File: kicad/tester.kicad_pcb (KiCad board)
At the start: 2 copper layers, 95 x 89 mm, 0 parts

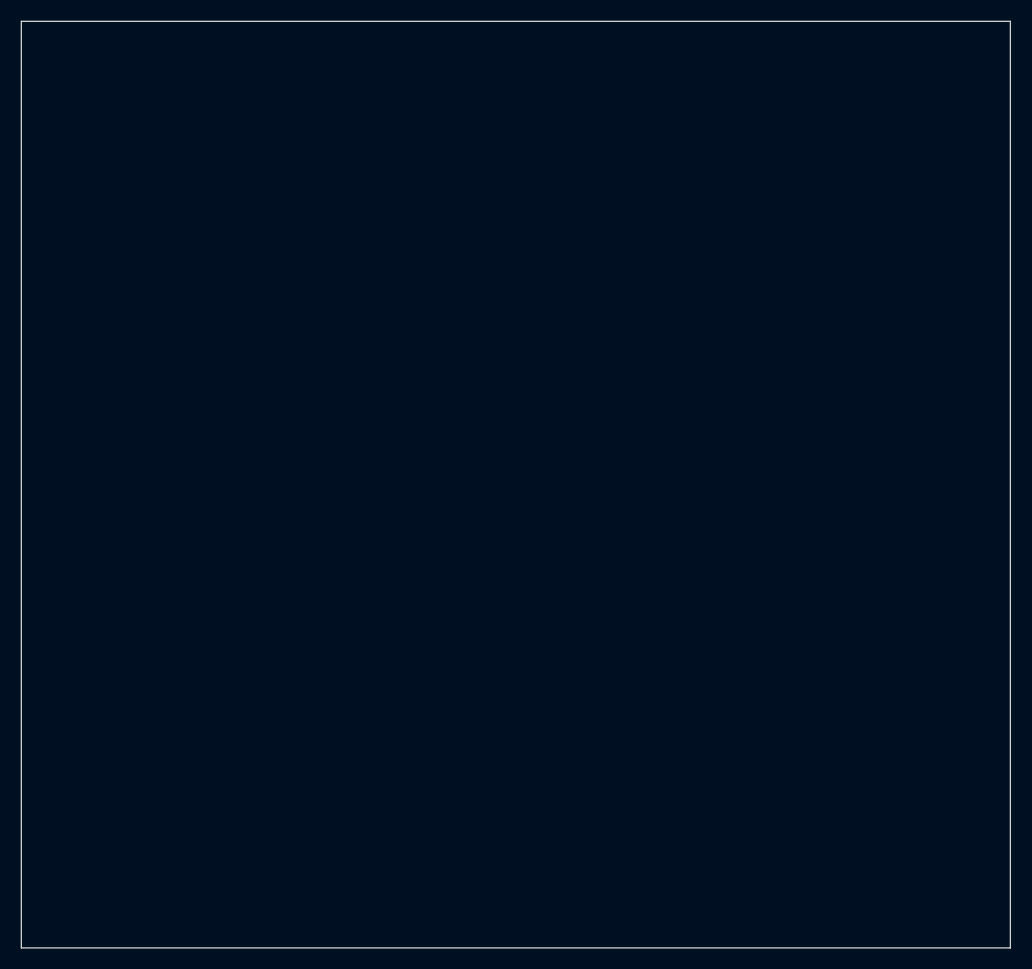
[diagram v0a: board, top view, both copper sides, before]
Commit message: Board routing almost done
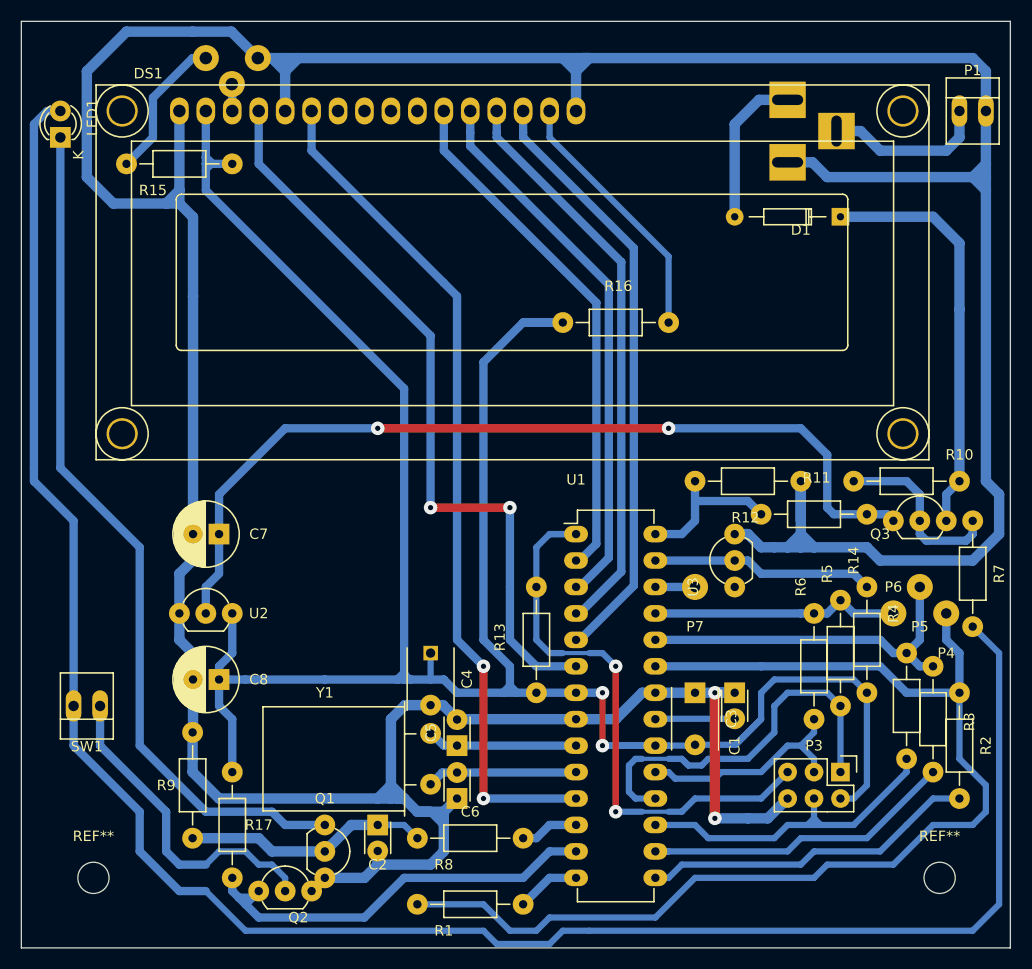
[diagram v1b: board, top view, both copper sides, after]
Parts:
- added C1: 1n, Capacitors_ThroughHole:C_Disc_D3_P2.5, F.Cu at (96.5, 110.5)
- added C2: 10n, Capacitors_ThroughHole:C_Disc_D3_P2.5, F.Cu at (62.2, 123.2)
- added C3: 100n, Capacitors_ThroughHole:C_Disc_D6_P5, F.Cu at (92.7, 110.5)
- added C4: 100n, Capacitors_ThroughHole:C_Disc_D6_P5, F.Cu at (67.3, 106.7)
- added C5: 22p, Capacitors_ThroughHole:C_Disc_D3_P2.5, F.Cu at (69.8, 115.6)
- added C6: 22p, Capacitors_ThroughHole:C_Disc_D3_P2.5, F.Cu at (69.8, 120.7)
- added C7: 2.2uF, Capacitors_ThroughHole:C_Radial_D6.3_L11.2_P2.5, F.Cu at (47.0, 95.2)
- added C8: 2.2uF, Capacitors_ThroughHole:C_Radial_D6.3_L11.2_P2.5, F.Cu at (47.0, 109.2)
- added D1: D_Small, Diodes_ThroughHole:Diode_DO-35_SOD27_Horizontal_RM10, F.Cu at (106.7, 64.8)
- added DS1: LCD16X2, Display:WC1602A, F.Cu at (43.2, 54.6)
- added LED1: Power, LEDs:LED-3MM, F.Cu at (31.8, 57.1)
- added P1: Battery 9V, Connect:PINHEAD1-2, F.Cu at (119.4, 54.6)
- added P2: 7-12 DC, Connect:BARREL_JACK, B.Cu at (101.6, 53.3)
- added P3: ISP, Pin_Headers:Pin_Header_Straight_2x03, F.Cu at (106.7, 118.1)
- added P4: TP1, Wire_Pads:SolderWirePad_single_1mmDrill, F.Cu at (116.8, 102.9)
- added P5: TP2, Wire_Pads:SolderWirePad_single_1mmDrill, F.Cu at (114.3, 100.3)
- added P6: TP3, Wire_Pads:SolderWirePad_single_1mmDrill, F.Cu at (111.8, 102.9)
- added P7: SERIAL, Wire_Pads:SolderWirePad_single_1mmDrill, F.Cu at (92.7, 100.3)
- added Q1: BC547, TO_SOT_Packages_THT:TO-92_Inline_Wide, F.Cu at (57.1, 123.2)
- added Q2: BC547, TO_SOT_Packages_THT:TO-92_Inline_Wide, F.Cu at (50.8, 129.5)
- added Q3: BC557, TO_SOT_Packages_THT:TO-92_Inline_Wide, F.Cu at (111.8, 94.0)
- added R1: 680, Resistors_ThroughHole:Resistor_Horizontal_RM10mm, F.Cu at (66.0, 130.8)
- added R10: 33K, Resistors_ThroughHole:Resistor_Horizontal_RM10mm, F.Cu at (118.1, 90.2)
- added R11: 10K, Resistors_ThroughHole:Resistor_Horizontal_RM10mm, F.Cu at (99.1, 93.3)
- added R12: 3K3, Resistors_ThroughHole:Resistor_Horizontal_RM10mm, F.Cu at (102.9, 90.2)
- added R13: 10k, Resistors_ThroughHole:Resistor_Horizontal_RM10mm, F.Cu at (77.5, 110.5)
- added R14: 2K2, Resistors_ThroughHole:Resistor_Horizontal_RM10mm, F.Cu at (109.2, 100.3)
- added R15: 10K, Resistors_ThroughHole:Resistor_Horizontal_RM10mm, F.Cu at (48.3, 59.7)
- added R16: 270, Resistors_ThroughHole:Resistor_Horizontal_RM10mm, F.Cu at (80.0, 74.9)
- added R17: 27K, Resistors_ThroughHole:Resistor_Horizontal_RM10mm, F.Cu at (48.3, 118.1)
- added R2: 470K, Resistors_ThroughHole:Resistor_Horizontal_RM10mm, F.Cu at (118.1, 110.5)
- added R3: 680, Resistors_ThroughHole:Resistor_Horizontal_RM10mm, F.Cu at (115.6, 108.0)
- added R4: 470K, Resistors_ThroughHole:Resistor_Horizontal_RM10mm, F.Cu at (113.0, 106.7)
- added R5: 680, Resistors_ThroughHole:Resistor_Horizontal_RM10mm, F.Cu at (106.7, 101.6)
- added R6: 470K, Resistors_ThroughHole:Resistor_Horizontal_RM10mm, F.Cu at (104.1, 102.9)
- added R7: 3K3, Resistors_ThroughHole:Resistor_Horizontal_RM10mm, F.Cu at (119.4, 94.0)
- added R8: 27K, Resistors_ThroughHole:Resistor_Horizontal_RM10mm, F.Cu at (66.0, 124.5)
- added R9: 100K, Resistors_ThroughHole:Resistor_Horizontal_RM10mm, F.Cu at (44.5, 124.5)
- added REF**: MountingHole_3mm, Mounting_Holes:MountingHole_3mm, F.Cu at (34.9, 128.3)
- added REF**: MountingHole_3mm, Mounting_Holes:MountingHole_3mm, F.Cu at (116.2, 128.3)
- added RV1: 5K, Potentiometers:Potentiometer_VishaySpectrol-Econtrim-Type36k, B.Cu at (45.7, 49.5)
- added SW1: TEST, Connect:PINHEAD1-2, F.Cu at (34.3, 111.8)
- added U1: ATMEGA328-P, Housings_DIP:DIP-28_W7.62mm_LongPads, F.Cu at (81.3, 95.2)
- added U2: MCP1702-5002E/TO, TO_SOT_Packages_THT:TO-92_Inline_Wide, F.Cu at (43.2, 102.9)
- added U3: LM336, TO_SOT_Packages_THT:TO-92_Inline_Wide, F.Cu at (96.5, 100.3)
- added Y1: 8MHz, Crystals:Crystal_HC49-U_Horizontal_Typ1, F.Cu at (67.3, 116.8)
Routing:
- net GND: track 0.00 -> 423.3 mm, vias 0 -> 2
- net VCC: track 0.00 -> 234.9 mm, vias 0 -> 2
- net Net-(LED1-Pad2): track 0.00 -> 192.7 mm
- net Net-(P4-Pad1): track 0.00 -> 111.3 mm
- net +9V: track 0.00 -> 86.0 mm, vias 0 -> 2
- net Net-(LED1-Pad1): track 0.00 -> 82.5 mm
- net Net-(DS1-Pad6): track 0.00 -> 82.1 mm, vias 0 -> 2
- net Net-(DS1-Pad4): track 0.00 -> 73.0 mm, vias 0 -> 2
- net Net-(DS1-Pad14): track 0.00 -> 57.7 mm
- net /RESET: track 0.00 -> 56.5 mm, vias 0 -> 2
- net Net-(DS1-Pad13): track 0.00 -> 55.2 mm
- net Net-(Q2-Pad1): track 0.00 -> 53.7 mm
- net Net-(DS1-Pad12): track 0.00 -> 52.7 mm
- net Net-(DS1-Pad11): track 0.00 -> 50.3 mm
- net Net-(D1-Pad1): track 0.00 -> 39.7 mm
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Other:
- net class Default: trace_width 0.25 -> 0.8
- net class Power added: clearance 0.2, trace_width 1, via_dia 1.3, via_drill 0.5
- net class Smaller added: clearance 0.2, trace_width 0.6, via_dia 0.6, via_drill 0.4

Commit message: * Minor changes
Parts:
- moved C8 19.4 mm to (57.1, 92.7)
- moved D1 14.4 mm to (96.5, 74.9), turned to 90 degrees
- moved C7 2.54 mm to (47.0, 92.7)
- moved U2 2.54 mm to (43.2, 100.3)
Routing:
- net GND: track 423.3 -> 461.8 mm
- net VCC: track 234.9 -> 261.5 mm
- net +9V: track 86.0 -> 85.0 mm
- net /Bat+: track 15.7 -> 16.7 mm
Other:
- net class Power2 added: clearance 0.2, trace_width 1.8, via_dia 0.6, via_drill 0.4

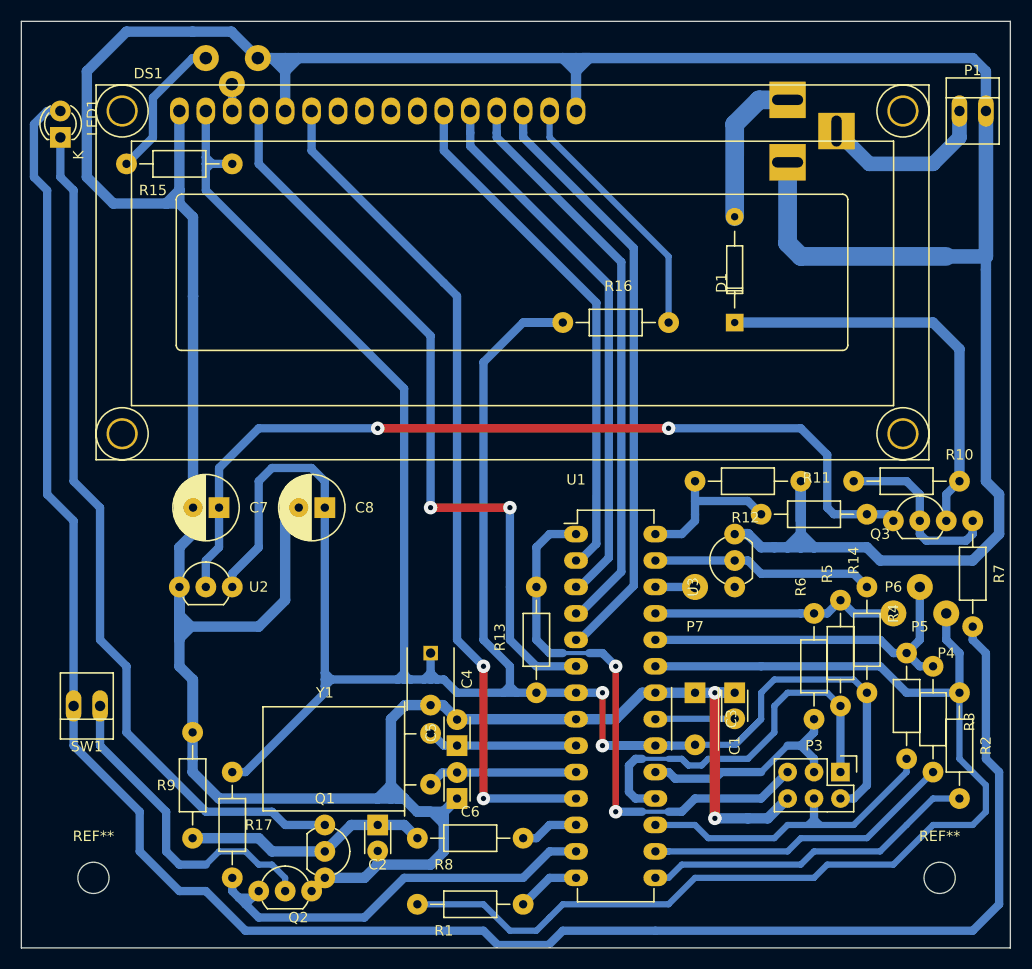
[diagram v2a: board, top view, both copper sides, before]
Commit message: * Adds teardrop * Minor improvements
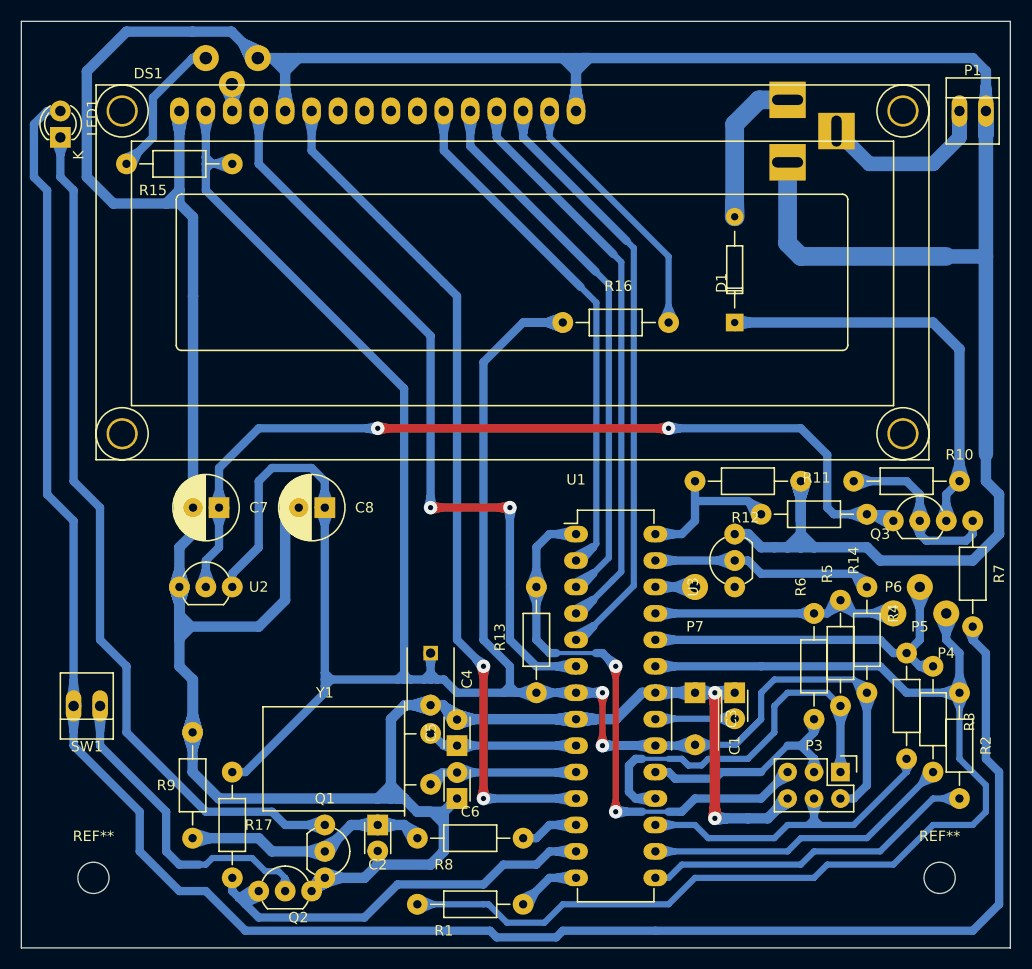
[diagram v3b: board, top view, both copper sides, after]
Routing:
- net Net-(Q2-Pad1): track 53.7 -> 42.3 mm
- net Net-(P4-Pad1): track 111.3 -> 110.6 mm
- net Net-(LED1-Pad2): track 192.7 -> 192.1 mm
- net Net-(Q2-Pad2): track 31.4 -> 30.9 mm
